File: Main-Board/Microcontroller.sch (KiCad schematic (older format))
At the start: 32 parts, among them J8 USB_B_Micro, J9 ICSP, SW1 Reset, U3 FT232RL, U4 ATmega328P-AU, U5 LM1117-5.0, Y1 16 MHz

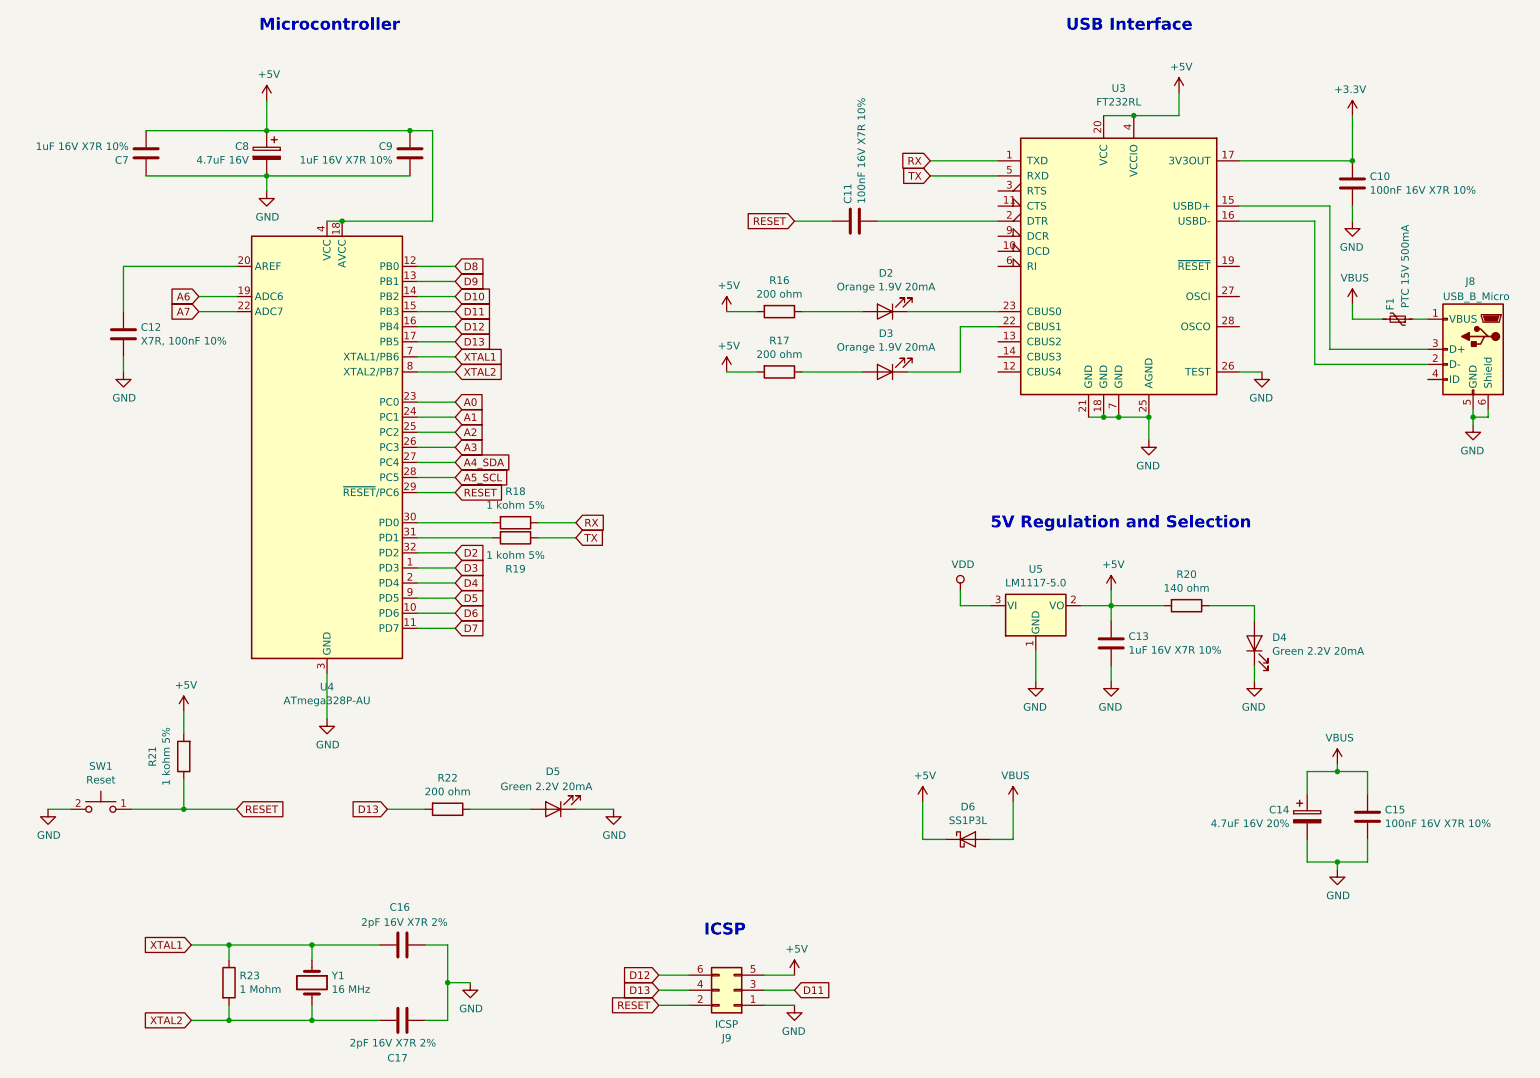
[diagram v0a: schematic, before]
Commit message: Reviewed MCU. Next have to generate BOM and route board
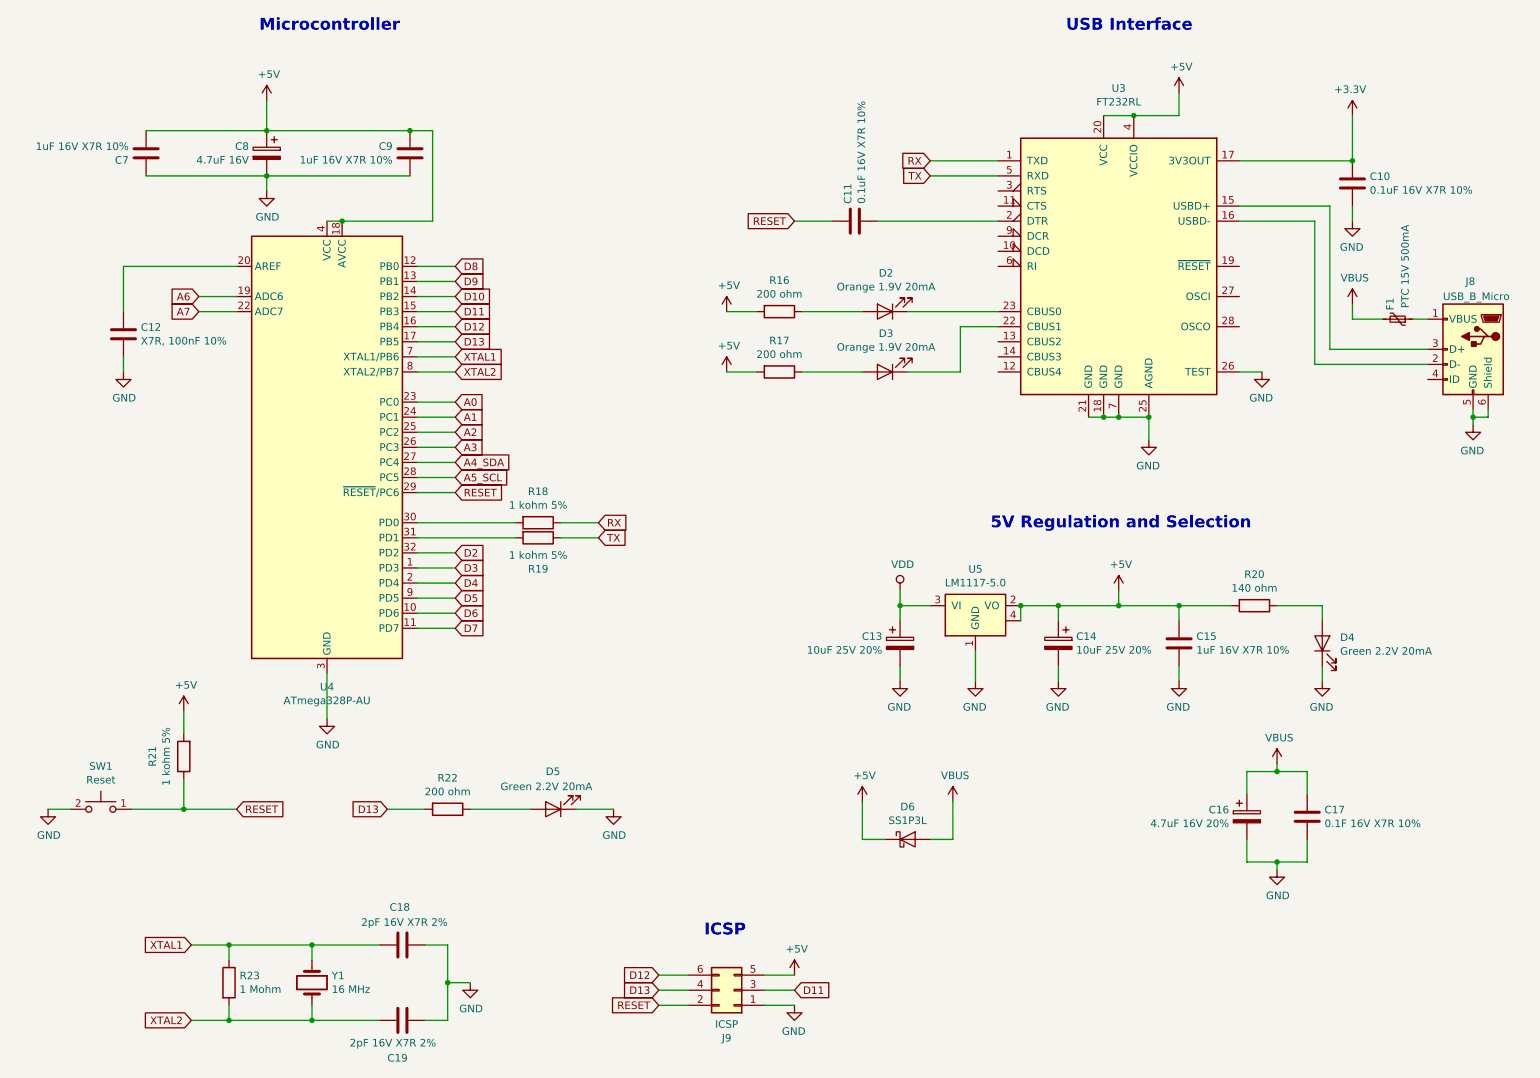
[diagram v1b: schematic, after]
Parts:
- removed U5: LM1117-5.0, Package_TO_SOT_SMD:SOT-223, symbol Regulator_Linear:LM1117-5.0
- added C13, C14: 10uF 25V 20%, Capacitor_SMD:C_0603_1608Metric_Pad1.05x0.95mm_HandSolder, symbol Device:CP
- added U5: LM1117-5.0, Package_TO_SOT_SMD:SOT-223, symbol Custom:LM1117-5.0
- C10, C11: value 100nF 16V X7R 10% -> 0.1uF 16V X7R 10%
- C17: renamed from C15; value 100nF 16V X7R 10% -> 0.1F 16V X7R 10%
- D6: Digi-Key # (none) -> MSS1P3LHM3_A/HGICT-ND; Digi-Key LinkDigi LinkDigi-Key Link (none) -> https://www.digikey.ca/en/products/detail/vishay-semiconduc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; Manufacturer (none) -> Vishay Semiconductor Diodes Division; Manufacturer # (none) -> MSS1P3LHM3_A/H
- SW1: Digi-Key # (none) -> CKN10361CT-ND; Digi-Key LinkDigi LinkDigi-Key Link (none) -> https://www.digikey.ca/en/products/detail/c-k/RS-187R05A2-D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; Manufacturer (none) -> C&K; Manufacturer # (none) -> RS-187R05A2-DS MT RT
- U4: Digi-Key # (none) -> ATMEGA328P-AU-ND; Digi-Key LinkDigi LinkDigi-Key Link (none) -> https://www.digikey.ca/en/products/detail/microchip-technol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; Manufacturer (none) -> Microchip Technology; Manufacturer # (none) -> ATMEGA328P-AU
- Y1: footprint Crystal:Resonator-2Pin_W10.0mm_H5.0mm -> Custom:Crystal; Manufacturer # CRYSTAL 16.0000MHZ 20PF TH -> FC4STCBMF16.0-BAG200
- renumbered C13 to C15, C14 to C16, C16 to C18, C17 to C19
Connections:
- net +5V: now also C14.1, U5.2 (VO), U5.4
- net GND: now also C13.2, C14.2, U5.1 (GND)
- net VDD: now also C13.1, U5.3 (VI)
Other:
- moved on the sheet: C15, C16, C17, D4, D6, R18, R19, R20

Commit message: Minor updates for components to reflect BOM
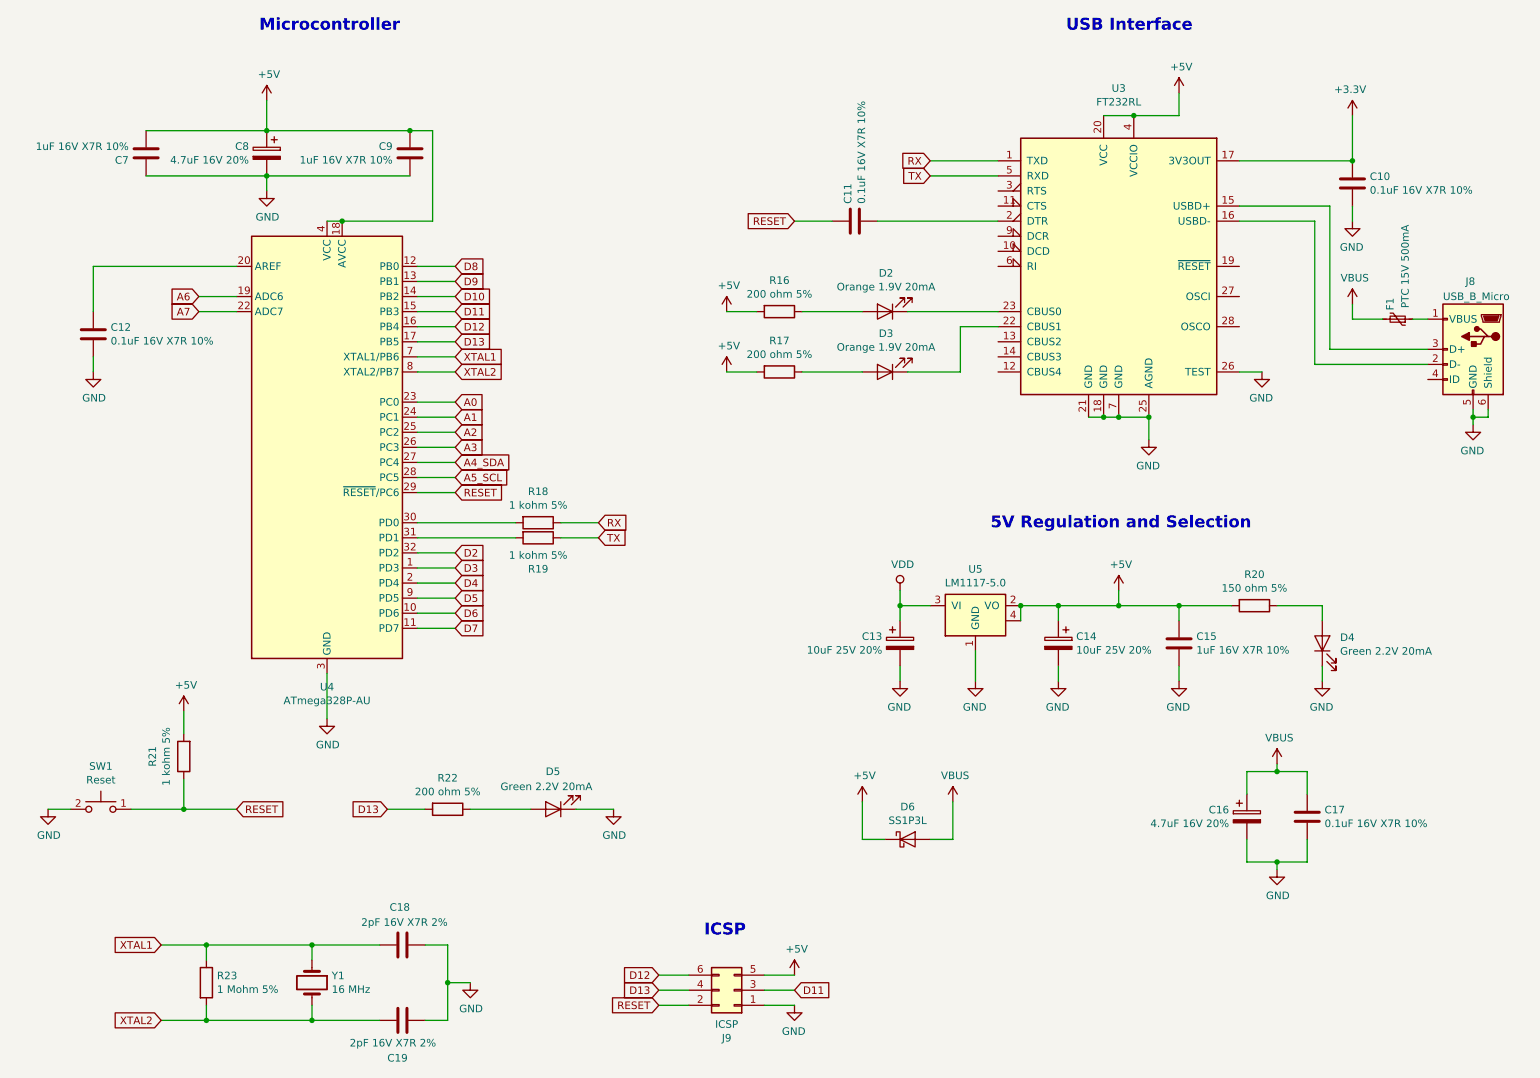
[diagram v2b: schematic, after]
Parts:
- C12: value X7R, 100nF 10% -> 0.1uF 16V X7R 10%
- C17: value 0.1F 16V X7R 10% -> 0.1uF 16V X7R 10%
- C8: value 4.7uF 16V -> 4.7uF 16V 20%
- F1: Digi-Key # (none) -> 283-3140-1-ND; Digi-Key LinkDigi LinkDigi-Key Link (none) -> https://www.digikey.ca/en/products/detail/eaton-electronics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; Manufacturer (none) -> Eaton - Electronics Division; Manufacturer # (none) -> PTS120615V050
- R16, R17, R22: value 200 ohm -> 200 ohm 5%
- R20: value 140 ohm -> 150 ohm 5%
- R23: value 1 Mohm -> 1 Mohm 5%
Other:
- moved on the sheet: C12, R23
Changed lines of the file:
@@
 Sheet 3 3
 Title "Microcontroller"
-Date "2020-12-20"
+Date "2020-12-21"
 Rev "A"
 Comp ""
@@
 F 2 "Fuse:Fuse_1206_3216Metric_Pad1.42x1.75mm_HandSolder" H 9750 2450 50  0001 L CNN
 F 3 "~" H 9700 2650 50  0001 C CNN
+F 4 "Eaton - Electronics Division" H 9700 2650 50  0001 C CNN "Manufacturer"
+F 5 "PTS120615V050" H 9700 2650 50  0001 C CNN "Manufacturer #"
+F 6 "283-3140-1-ND" H 9700 2650 50  0001 C CNN "Digi-Key #"
+F 7 "https://www.digikey.ca/en/products/detail/eaton-electronics-division/PTS120615V050/2639137" H 9700 2650 50  0001 C CNN "Digi-Key LinkDigi LinkDigi-Key Link"
 	1    9700 2650
 	0    1    -1   0
@@
 P 5600 2600
 F 0 "R16" V 5393 2600 50  0000 C CNN
-F 1 "200 ohm" V 5484 2600 50  0000 C CNN
+F 1 "200 ohm 5%" V 5484 2600 50  0000 C CNN
 F 2 "Resistor_SMD:R_0603_1608Metric_Pad1.05x0.95mm_HandSolder" V 5530 2600 50  0001 C CNN
 F 3 "~" H 5600 2600 50  0001 C CNN
@@
 AR Path="/5FDD4B9C/5FE1D929" Ref="C17"  Part="1"
 F 0 "C17" H 9215 5996 50  0000 L CNN
-F 1 "0.1F 16V X7R 10%" H 9215 5905 50  0000 L CNN
+F 1 "0.1uF 16V X7R 10%" H 9215 5905 50  0000 L CNN
 F 2 "Capacitor_SMD:C_0603_1608Metric_Pad1.05x0.95mm_HandSolder" H 9138 5800 50  0001 C CNN
 F 3 "~" H 9100 5950 50  0001 C CNN
@@
 P 8750 4550
 F 0 "R20" V 8543 4550 50  0000 C CNN
-F 1 "140 ohm" V 8634 4550 50  0000 C CNN
+F 1 "150 ohm 5%" V 8634 4550 50  0000 C CNN
 F 2 "Resistor_SMD:R_0603_1608Metric_Pad1.05x0.95mm_HandSolder" V 8680 4550 50  0001 C CNN
 F 3 "~" H 8750 4550 50  0001 C CNN
@@
 L Device:C C?
 U 1 1 5FF2F0D6
-P 1250 2750
+P 1050 2750
 AR Path="/5FD99B6C/5FF2F0D6" Ref="C?"  Part="1"
 AR Path="/5FD9E07D/5FF2F0D6" Ref="C?"  Part="1"
 AR Path="/5FDD4B9C/5FF2F0D6" Ref="C12"  Part="1"
-F 0 "C12" H 1365 2796 50  0000 L CNN
-F 1 "X7R, 100nF 10%" H 1365 2705 50  0000 L CNN
-F 2 "Capacitor_SMD:C_0603_1608Metric_Pad1.05x0.95mm_HandSolder" H 1288 2600 50  0001 C CNN
-F 3 "~" H 1250 2750 50  0001 C CNN
-	1    1250 2750
-	1    0    0    -1
-$EndComp
-Wire Wire Line
-	1250 2600 1250 2300
-Wire Wire Line
-	1250 2300 2000 2300
+F 0 "C12" H 1165 2796 50  0000 L CNN
+F 1 "0.1uF 16V X7R 10%" H 1165 2705 50  0000 L CNN
+F 2 "Capacitor_SMD:C_0603_1608Metric_Pad1.05x0.95mm_HandSolder" H 1088 2600 50  0001 C CNN
+F 3 "~" H 1050 2750 50  0001 C CNN
+	1    1050 2750
+	1    0    0    -1
+$EndComp
+Wire Wire Line
+	1050 2600 1050 2300
 $Comp
 L power:GND #PWR?
 U 1 1 5FF3E163
-P 1250 3000
+P 1050 3000
 AR Path="/5FF3E163" Ref="#PWR?"  Part="1"
 AR Path="/5FDD4B9C/5FF3E163" Ref="#PWR044"  Part="1"
-F 0 "#PWR044" H 1250 2750 50  0001 C CNN
-F 1 "GND" H 1255 2827 50  0000 C CNN
-F 2 "" H 1250 3000 50  0001 C CNN
-F 3 "" H 1250 3000 50  0001 C CNN
-	1    1250 3000
-	1    0    0    -1
-$EndComp
-Wire Wire Line
-	1250 3000 1250 2900
+F 0 "#PWR044" H 1050 2750 50  0001 C CNN
+F 1 "GND" H 1055 2827 50  0000 C CNN
+F 2 "" H 1050 3000 50  0001 C CNN
+F 3 "" H 1050 3000 50  0001 C CNN
+	1    1050 3000
+	1    0    0    -1
+$EndComp
+Wire Wire Line
+	1050 3000 1050 2900
 Wire Wire Line
 	3450 2800 3200 2800
@@
 P 2200 1550
 F 0 "C8" H 2318 1596 50  0000 L CNN
-F 1 "4.7uF 16V" H 2318 1505 50  0000 L CNN
+F 1 "4.7uF 16V 20%" H 2318 1505 50  0000 L CNN
 F 2 "Capacitor_SMD:C_0603_1608Metric_Pad1.05x0.95mm_HandSolder" H 2238 1400 50  0001 C CNN
 F 3 "~" H 2200 1550 50  0001 C CNN
@@
 P 5600 3000
 F 0 "R17" V 5393 3000 50  0000 C CNN
-F 1 "200 ohm" V 5484 3000 50  0000 C CNN
+F 1 "200 ohm 5%" V 5484 3000 50  0000 C CNN
 F 2 "Resistor_SMD:R_0603_1608Metric_Pad1.05x0.95mm_HandSolder" V 5530 3000 50  0001 C CNN
 F 3 "~" H 5600 3000 50  0001 C CNN
@@
 P 3400 5900
 F 0 "R22" V 3193 5900 50  0000 C CNN
-F 1 "200 ohm" V 3284 5900 50  0000 C CNN
+F 1 "200 ohm 5%" V 3284 5900 50  0000 C CNN
 F 2 "Resistor_SMD:R_0603_1608Metric_Pad1.05x0.95mm_HandSolder" V 3330 5900 50  0001 C CNN
 F 3 "~" H 3400 5900 50  0001 C CNN
@@
 L Device:R R23
 U 1 1 60339A37
-P 1950 7050
-F 0 "R23" H 2020 7096 50  0000 L CNN
-F 1 "1 Mohm" H 2020 7005 50  0000 L CNN
-F 2 "Resistor_SMD:R_0603_1608Metric_Pad1.05x0.95mm_HandSolder" V 1880 7050 50  0001 C CNN
-F 3 "~" H 1950 7050 50  0001 C CNN
-	1    1950 7050
+P 1800 7050
+F 0 "R23" H 1870 7096 50  0000 L CNN
+F 1 "1 Mohm 5%" H 1870 7005 50  0000 L CNN
+F 2 "Resistor_SMD:R_0603_1608Metric_Pad1.05x0.95mm_HandSolder" V 1730 7050 50  0001 C CNN
+F 3 "~" H 1800 7050 50  0001 C CNN
+	1    1800 7050
 	1    0    0    -1
 $EndComp
@@
 $EndComp
 Wire Wire Line
-	1950 6900 1950 6800
-Wire Wire Line
-	1950 6800 2500 6800
-Wire Wire Line
-	1950 7300 1950 7200
+	1800 6900 1800 6800
+Wire Wire Line
+	1800 7300 1800 7200
 Wire Wire Line
 	2500 7200 2500 7300
-Wire Wire Line
-	2500 7300 1950 7300
 Wire Wire Line
 	2500 6900 2500 6800
@@
 	2950 6800 2500 6800
 Connection ~ 2500 6800
-Text GLabel 1700 6800 0    50   Input ~ 0
+Text GLabel 1500 6800 0    50   Input ~ 0
 XTAL1
-Text GLabel 1700 7300 0    50   Input ~ 0
+Text GLabel 1500 7300 0    50   Input ~ 0
 XTAL2
-Wire Wire Line
-	1700 6800 1950 6800
-Connection ~ 1950 6800
-Wire Wire Line
-	1950 7300 1700 7300
-Connection ~ 1950 7300
 $Comp
 L Custom:Push-Switch SW1
@@
 Wire Wire Line
 	7850 4550 8250 4550
+Connection ~ 1800 6800
+Connection ~ 1800 7300
+Wire Wire Line
+	1800 6800 2500 6800
+Wire Wire Line
+	1800 7300 2500 7300
+Wire Wire Line
+	1500 6800 1800 6800
+Wire Wire Line
+	1500 7300 1800 7300
+Wire Wire Line
+	1050 2300 2000 2300
 $EndSCHEMATC
